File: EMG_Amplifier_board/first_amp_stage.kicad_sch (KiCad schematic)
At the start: 12 parts, among them U2 INA333xxDGK, U3 LPV821DBVR

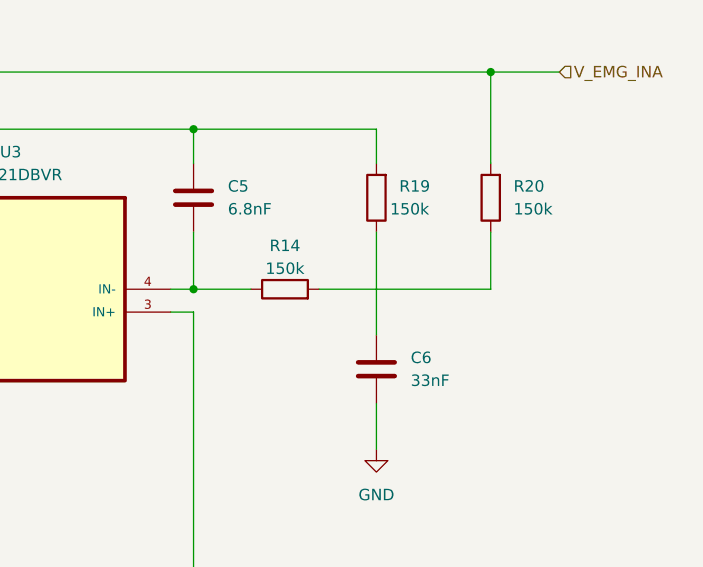
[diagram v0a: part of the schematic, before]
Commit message: correct the 400Hz LPF schematic and InAmp trace routing
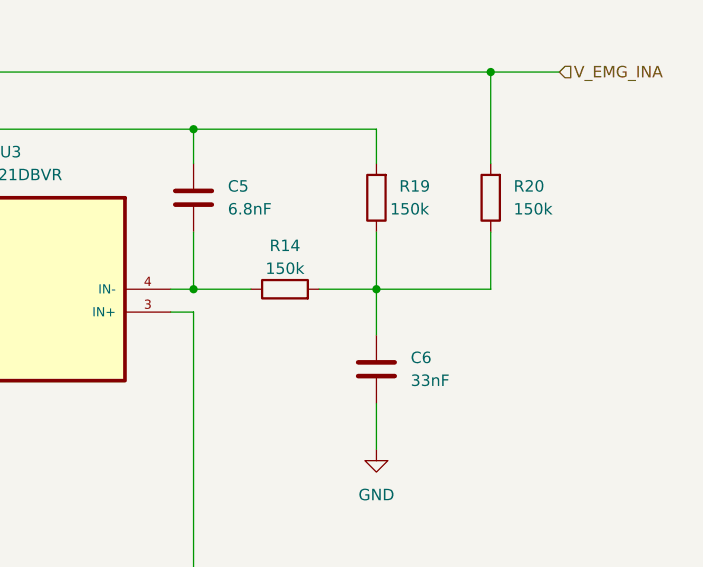
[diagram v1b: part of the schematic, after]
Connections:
- net at R14.2, R20.1: now also C6.1, R19.1
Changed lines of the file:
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@@
+	)
+	(junction
+		(at 186.69 80.01)
+		(diameter 0)
+		(color 0 0 0 0)
 	)
 	(junction
@@
 	(wire
 		(pts
+			(xy 180.34 80.01) (xy 186.69 80.01)
+		)
+		(stroke
+			(width 0)
+			(type default)
+		)
+	)
+	(wire
+		(pts
 			(xy 128.27 72.39) (xy 119.38 72.39)
 		)
@@
 	(wire
 		(pts
-			(xy 186.69 73.66) (xy 186.69 85.09)
+			(xy 186.69 73.66) (xy 186.69 80.01)
 		)
 		(stroke
@@
 	(wire
 		(pts
+			(xy 186.69 80.01) (xy 199.39 80.01)
+		)
+		(stroke
+			(width 0)
+			(type default)
+		)
+	)
+	(wire
+		(pts
 			(xy 109.22 40.64) (xy 109.22 50.8)
 		)
@@
 	(wire
 		(pts
-			(xy 180.34 80.01) (xy 199.39 80.01)
-		)
-		(stroke
-			(width 0)
-			(type default)
-		)
-	)
-	(wire
-		(pts
 			(xy 124.46 82.55) (xy 121.92 82.55)
 		)
@@
 		)
 		(stroke
+			(width 0)
+			(type default)
+		)
+	)
+	(wire
+		(pts
+			(xy 186.69 80.01) (xy 186.69 85.09)
+		)
+		(stroke

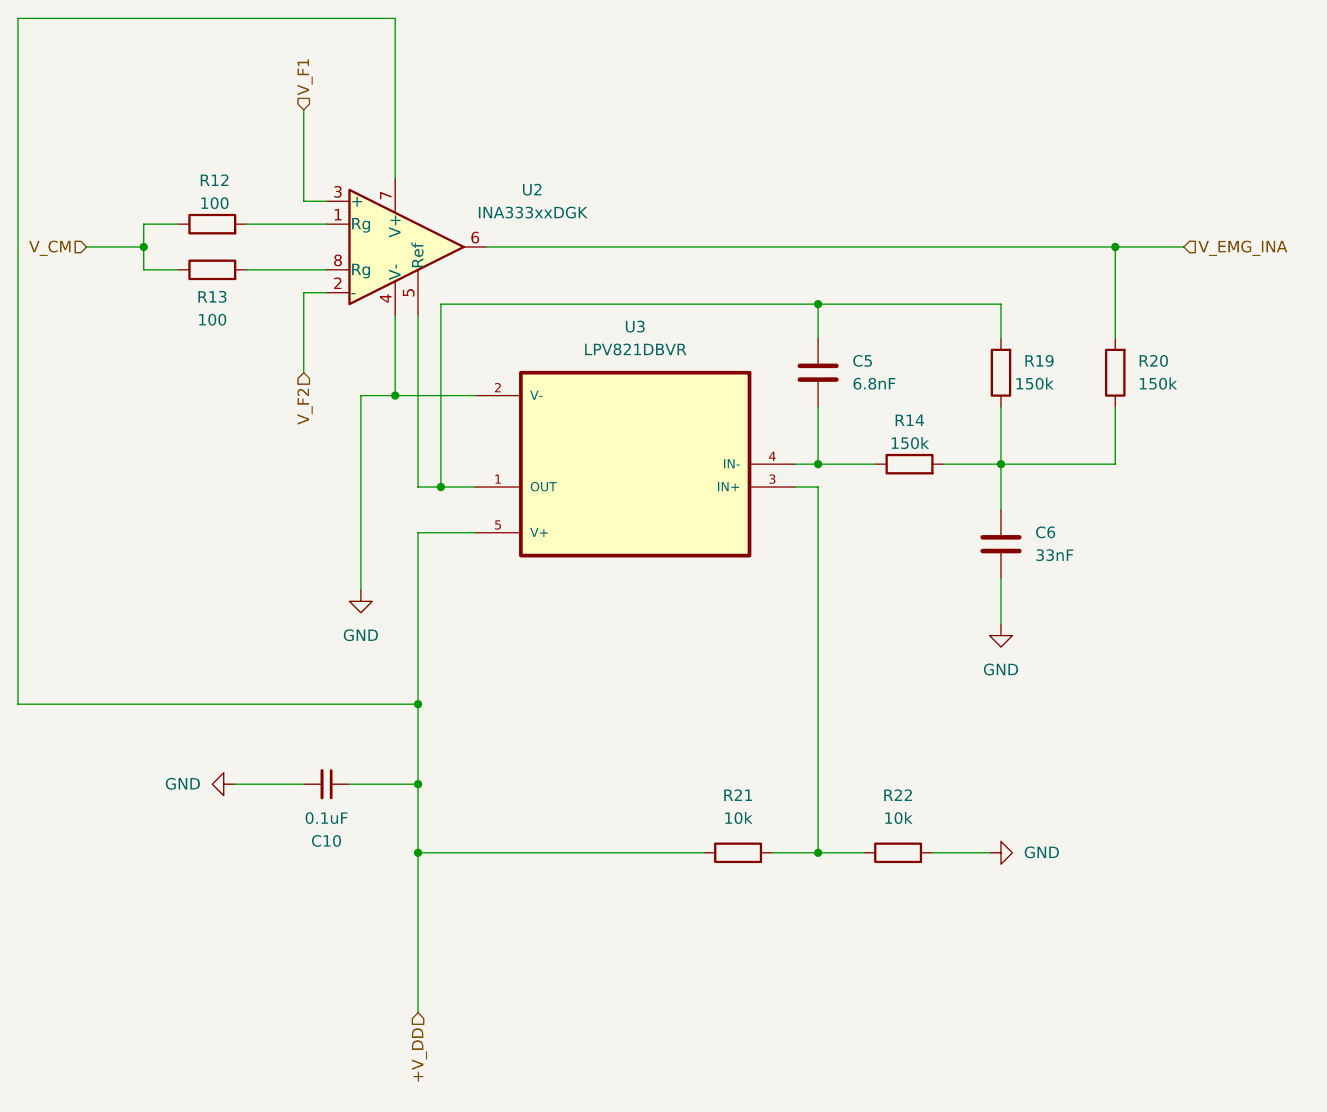
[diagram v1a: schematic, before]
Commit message: update R and C refs to correspond to paper
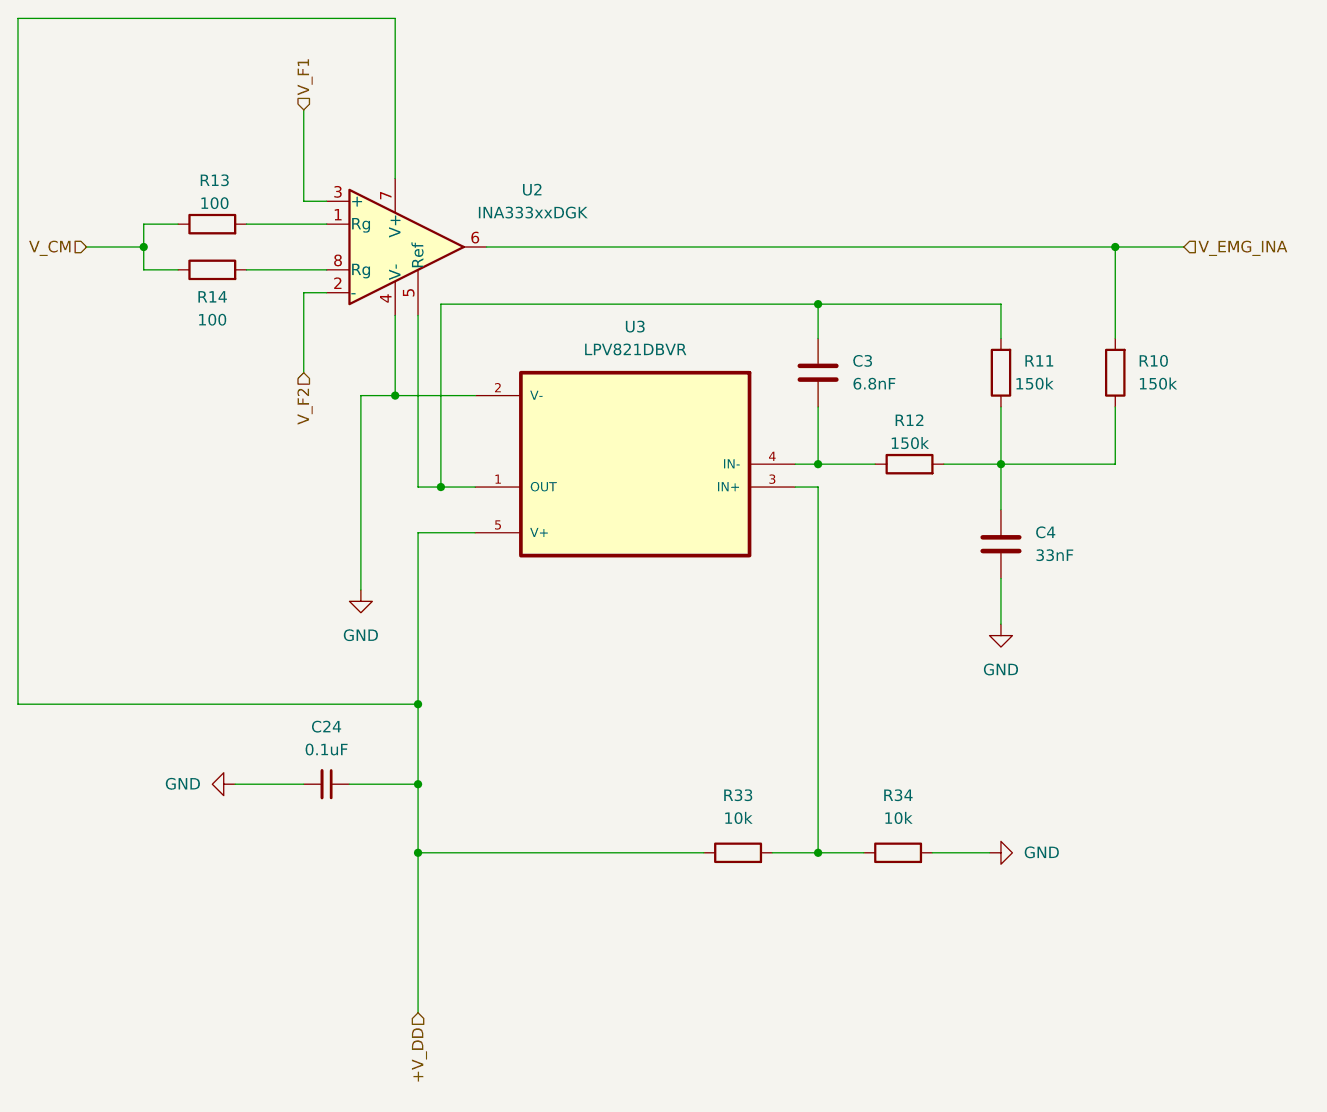
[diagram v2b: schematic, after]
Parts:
- renumbered C10 to C24, C5 to C3, C6 to C4, R20 to R10, R19 to R11, R14 to R12, R12 to R13, R13 to R14, R21 to R33, R22 to R34
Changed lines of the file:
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@@
 		(dnp no)
 		(fields_autoplaced yes)
-		(property "Reference" "R21"
+		(property "Reference" "R33"
 			(at 157.48 116.84 90)
 			(effects
@@
 			(project ""
 				(path "/26861adc-1ddf-4c37-9f8b-8db1c0839771/190e8daf-ffdb-4cbc-86a8-05377b040767/ee6da384-2a51-46fd-9ef1-0e50994f466c"
-					(reference "R21")
+					(reference "R33")
 					(unit 1)
 				)
@@
 		(on_board yes)
 		(dnp no)
-		(property "Reference" "R13"
+		(property "Reference" "R14"
 			(at 99.06 61.468 90)
 			(effects
@@
 			(project "EMG_amplifier"
 				(path "/26861adc-1ddf-4c37-9f8b-8db1c0839771/190e8daf-ffdb-4cbc-86a8-05377b040767/ee6da384-2a51-46fd-9ef1-0e50994f466c"
-					(reference "R13")
+					(reference "R14")
 					(unit 1)
 				)
@@
 		(dnp no)
 		(fields_autoplaced yes)
-		(property "Reference" "C10"
-			(at 111.7537 121.92 90)
+		(property "Reference" "C24"
+			(at 111.7536 109.22 90)
 			(effects
 				(font
@@
 		)
 		(property "Value" "0.1uF"
-			(at 111.7537 119.38 90)
+			(at 111.7536 111.76 90)
 			(effects
 				(font
@@
 			(project "EMG_amplifier"
 				(path "/26861adc-1ddf-4c37-9f8b-8db1c0839771/190e8daf-ffdb-4cbc-86a8-05377b040767/ee6da384-2a51-46fd-9ef1-0e50994f466c"
-					(reference "C10")
+					(reference "C24")
 					(unit 1)
 				)
@@
 		(dnp no)
 		(fields_autoplaced yes)
-		(property "Reference" "R22"
+		(property "Reference" "R34"
 			(at 175.26 116.84 90)
 			(effects
@@
 			(project ""
 				(path "/26861adc-1ddf-4c37-9f8b-8db1c0839771/190e8daf-ffdb-4cbc-86a8-05377b040767/ee6da384-2a51-46fd-9ef1-0e50994f466c"
-					(reference "R22")
+					(reference "R34")
 					(unit 1)
 				)
@@
 		(dnp no)
 		(fields_autoplaced yes)
-		(property "Reference" "R20"
+		(property "Reference" "R10"
 			(at 201.93 68.5799 0)
 			(effects
@@
 			(project "EMG_amplifier"
 				(path "/26861adc-1ddf-4c37-9f8b-8db1c0839771/190e8daf-ffdb-4cbc-86a8-05377b040767/ee6da384-2a51-46fd-9ef1-0e50994f466c"
-					(reference "R20")
+					(reference "R10")
 					(unit 1)
 				)
@@
 		(dnp no)
 		(fields_autoplaced yes)
-		(property "Reference" "C6"
+		(property "Reference" "C4"
 			(at 190.5 87.6299 0)
 			(effects
@@
 			(project "EMG_amplifier"
 				(path "/26861adc-1ddf-4c37-9f8b-8db1c0839771/190e8daf-ffdb-4cbc-86a8-05377b040767/ee6da384-2a51-46fd-9ef1-0e50994f466c"
-					(reference "C6")
+					(reference "C4")
 					(unit 1)
 				)
@@
 		(on_board yes)
 		(dnp no)
-		(property "Reference" "R19"
+		(property "Reference" "R11"
 			(at 189.23 68.5799 0)
 			(effects
@@
 			(project "EMG_amplifier"
 				(path "/26861adc-1ddf-4c37-9f8b-8db1c0839771/190e8daf-ffdb-4cbc-86a8-05377b040767/ee6da384-2a51-46fd-9ef1-0e50994f466c"
-					(reference "R19")
+					(reference "R11")
 					(unit 1)
 				)
@@
 		(dnp no)
 		(fields_autoplaced yes)
-		(property "Reference" "C5"
+		(property "Reference" "C3"
 			(at 170.18 68.5799 0)
 			(effects
@@
 			(project "EMG_amplifier"
 				(path "/26861adc-1ddf-4c37-9f8b-8db1c0839771/190e8daf-ffdb-4cbc-86a8-05377b040767/ee6da384-2a51-46fd-9ef1-0e50994f466c"
-					(reference "C5")
+					(reference "C3")
 					(unit 1)
 				)
@@
 		(on_board yes)
 		(dnp no)
-		(property "Reference" "R14"
+		(property "Reference" "R12"
 			(at 176.53 75.184 90)
 			(effects
@@
 			(project "EMG_amplifier"
 				(path "/26861adc-1ddf-4c37-9f8b-8db1c0839771/190e8daf-ffdb-4cbc-86a8-05377b040767/ee6da384-2a51-46fd-9ef1-0e50994f466c"
-					(reference "R14")
+					(reference "R12")
 					(unit 1)
 				)
@@
 		(on_board yes)
 		(dnp no)
-		(property "Reference" "R12"
+		(property "Reference" "R13"
 			(at 99.314 48.514 90)
 			(effects
@@
 			(project "EMG_amplifier"
 				(path "/26861adc-1ddf-4c37-9f8b-8db1c0839771/190e8daf-ffdb-4cbc-86a8-05377b040767/ee6da384-2a51-46fd-9ef1-0e50994f466c"
-					(reference "R12")
-					(unit 1)
-				)
+					(reference "R13")
+					(unit 1)
+				)

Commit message: replace 2012 capacitors with 1005
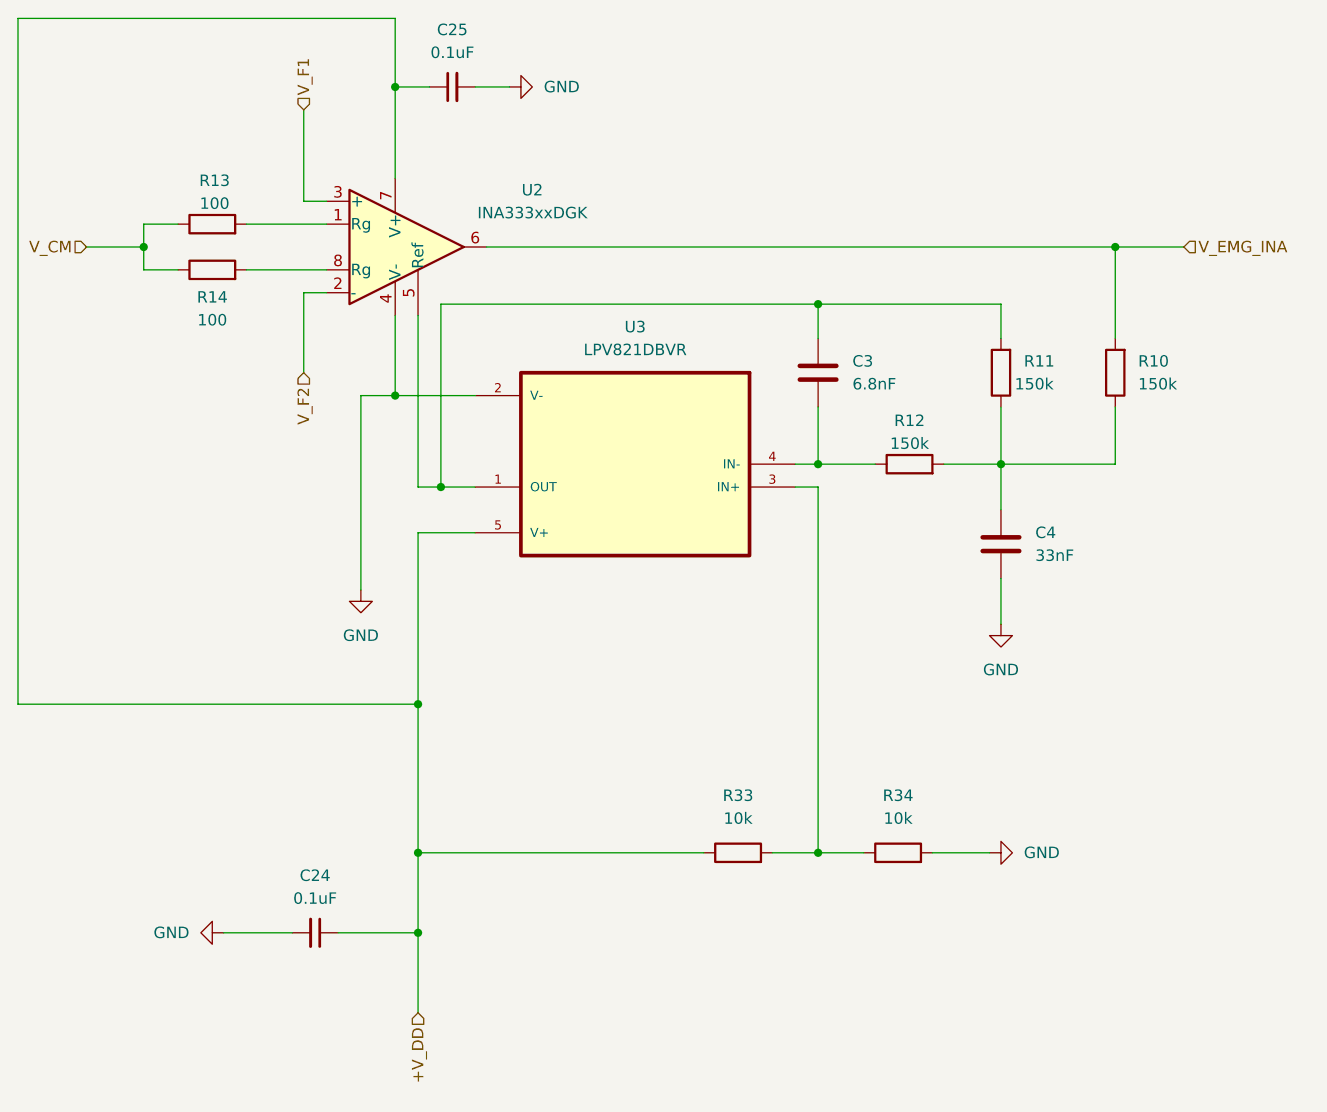
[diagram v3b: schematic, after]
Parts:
- added C25: 0.1uF, Capacitor_SMD:C_0402_1005Metric, symbol Device:C_Small
- C24: footprint Capacitor_SMD:C_0805_2012Metric -> Capacitor_SMD:C_0402_1005Metric
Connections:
- net +V_DD: now also C25.1
- net GND: now also C25.2
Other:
- moved on the sheet: C24
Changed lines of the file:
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@@
+	)
+	(junction
+		(at 121.92 132.08)
+		(diameter 0)
+		(color 0 0 0 0)
 	)
 	(junction
@@
 	)
 	(junction
-		(at 121.92 115.57)
+		(at 119.38 38.1)
 		(diameter 0)
 		(color 0 0 0 0)
@@
 	(wire
 		(pts
-			(xy 114.3 115.57) (xy 121.92 115.57)
+			(xy 119.38 38.1) (xy 119.38 48.26)
+		)
+		(stroke
+			(width 0)
+			(type default)
+		)
+	)
+	(wire
+		(pts
+			(xy 113.03 132.08) (xy 121.92 132.08)
 		)
 		(stroke
@@
 	(wire
 		(pts
-			(xy 121.92 123.19) (xy 121.92 140.97)
-		)
-		(stroke
-			(width 0)
-			(type default)
-		)
-	)
-	(wire
-		(pts
 			(xy 199.39 80.01) (xy 199.39 73.66)
 		)
@@
 	(wire
 		(pts
+			(xy 121.92 132.08) (xy 121.92 123.19)
+		)
+		(stroke
+			(width 0)
+			(type default)
+		)
+	)
+	(wire
+		(pts
 			(xy 199.39 55.88) (xy 199.39 66.04)
 		)
@@
 	(wire
 		(pts
+			(xy 121.92 132.08) (xy 121.92 140.97)
+		)
+		(stroke
+			(width 0)
+			(type default)
+		)
+	)
+	(wire
+		(pts
 			(xy 109.22 40.64) (xy 109.22 50.8)
 		)
@@
 	(wire
 		(pts
-			(xy 121.92 106.68) (xy 121.92 115.57)
-		)
-		(stroke
-			(width 0)
-			(type default)
-		)
-	)
-	(wire
-		(pts
-			(xy 119.38 30.48) (xy 119.38 48.26)
+			(xy 123.19 38.1) (xy 119.38 38.1)
+		)
+		(stroke
+			(width 0)
+			(type default)
+		)
+	)
+	(wire
+		(pts
+			(xy 119.38 30.48) (xy 119.38 38.1)
 		)
 		(stroke
@@
 	(wire
 		(pts
-			(xy 121.92 115.57) (xy 121.92 123.19)
+			(xy 121.92 106.68) (xy 121.92 123.19)
+		)
+		(stroke
+			(width 0)
+			(type default)
+		)
+	)
+	(wire
+		(pts
+			(xy 128.27 38.1) (xy 132.08 38.1)
 		)
 		(stroke
@@
 	(wire
 		(pts
-			(xy 109.22 115.57) (xy 101.6 115.57)
+			(xy 107.95 132.08) (xy 100.33 132.08)
 		)
 		(stroke
@@
 	(symbol
 		(lib_id "Device:C_Small")
-		(at 111.76 115.57 270)
+		(at 110.49 132.08 270)
 		(unit 1)
 		(exclude_from_sim no)
@@
 		(fields_autoplaced yes)
 		(property "Reference" "C24"
-			(at 111.7536 109.22 90)
+			(at 110.4836 125.73 90)
 			(effects
 				(font
@@
 		)
 		(property "Value" "0.1uF"
-			(at 111.7536 111.76 90)
-			(effects
-				(font
-					(size 1.27 1.27)
-				)
-			)
-		)
-		(property "Footprint" "Capacitor_SMD:C_0805_2012Metric"
-			(at 111.76 115.57 0)
+			(at 110.4836 128.27 90)
+			(effects
+				(font
+					(size 1.27 1.27)
+				)
+			)
+		)
+		(property "Footprint" "Capacitor_SMD:C_0402_1005Metric"
+			(at 110.49 132.08 0)
 			(effects
 				(font
@@
 		)
 		(property "Datasheet" "~"
-			(at 111.76 115.57 0)
+			(at 110.49 132.08 0)
 			(effects
 				(font
@@
 		)
 		(property "Description" "Unpolarized capacitor, small symbol"
-			(at 111.76 115.57 0)
+			(at 110.49 132.08 0)
 			(effects
 				(font
@@
 	)
 	(symbol
+		(lib_id "Device:C_Small")
+		(at 125.73 38.1 90)
+		(unit 1)
+		(exclude_from_sim no)
+		(in_bom yes)
+		(on_board yes)
+		(dnp no)
+		(fields_autoplaced yes)
+		(property "Reference" "C25"
+			(at 125.7363 31.75 90)
+			(effects
+				(font
+					(size 1.27 1.27)
+				)
+			)
+		)
+		(property "Value" "0.1uF"
+			(at 125.7363 34.29 90)
+			(effects
+				(font
+					(size 1.27 1.27)
+				)
+			)
+		)
+		(property "Footprint" "Capacitor_SMD:C_0402_1005Metric"
+			(at 125.73 38.1 0)
+			(effects
+				(font
+					(size 1.27 1.27)
+				)
+				(hide yes)
+			)
+		)
+		(property "Datasheet" "~"
+			(at 125.73 38.1 0)
+			(effects
+				(font
+					(size 1.27 1.27)
+				)
+				(hide yes)
+			)
+		)
+		(property "Description" "Unpolarized capacitor, small symbol"
+			(at 125.73 38.1 0)
+			(effects
+				(font
+					(size 1.27 1.27)
+				)
+				(hide yes)
+			)
+		)
+		(pin "1"
+		)
+		(pin "2"
+		)
+		(instances
+			(project "EMG_amplifier"
+				(path "/26861adc-1ddf-4c37-9f8b-8db1c0839771/190e8daf-ffdb-4cbc-86a8-05377b040767/ee6da384-2a51-46fd-9ef1-0e50994f466c"
+					(reference "C25")
+					(unit 1)
+				)
+			)
+		)
+	)
+	(symbol
 		(lib_id "LPV821DBVR:LPV821DBVR")
 		(at 146.05 80.01 180)
@@
 	(symbol
 		(lib_id "power:GND")
-		(at 101.6 115.57 270)
+		(at 100.33 132.08 270)
 		(unit 1)
 		(exclude_from_sim no)
@@
 		(fields_autoplaced yes)
 		(property "Reference" "#PWR010"
-			(at 95.25 115.57 0)
+			(at 93.98 132.08 0)
 			(effects
 				(font
@@
 		)
 		(property "Value" "GND"
-			(at 97.79 115.5701 90)
+			(at 96.52 132.0801 90)
 			(effects
 				(font
@@
 		)
 		(property "Footprint" ""
-			(at 101.6 115.57 0)
+			(at 100.33 132.08 0)
 			(effects
 				(font
@@
 		)
 		(property "Datasheet" ""
-			(at 101.6 115.57 0)
+			(at 100.33 132.08 0)
 			(effects
 				(font
@@
 		)
 		(property "Description" "Power symbol creates a global label with name \"GND\" , ground"
-			(at 101.6 115.57 0)
+			(at 100.33 132.08 0)
 			(effects
 				(font
@@
 					(unit 1)
 				)
+			)
+		)
+	)
+	(symbol
+		(lib_id "power:GND")
+		(at 132.08 38.1 90)
+		(unit 1)
+		(exclude_from_sim no)
+		(in_bom yes)
+		(on_board yes)
+		(dnp no)
+		(fields_autoplaced yes)
+		(property "Reference" "#PWR023"
+			(at 138.43 38.1 0)
+			(effects
+				(font
+					(size 1.27 1.27)
+				)
+				(hide yes)
+			)
+		)
+		(property "Value" "GND"
+			(at 135.89 38.0999 90)
+			(effects
+				(font
+					(size 1.27 1.27)
+				)
+				(justify right)
+			)
+		)
+		(property "Footprint" ""
+			(at 132.08 38.1 0)
+			(effects
+				(font
+					(size 1.27 1.27)
+				)
+				(hide yes)
+			)
+		)
+		(property "Datasheet" ""
+			(at 132.08 38.1 0)
+			(effects
+				(font
+					(size 1.27 1.27)
+				)
+				(hide yes)
+			)
+		)
+		(property "Description" "Power symbol creates a global label with name \"GND\" , ground"
+			(at 132.08 38.1 0)
+			(effects
+				(font
+					(size 1.27 1.27)
+				)
+				(hide yes)
+			)
+		)
+		(pin "1"
+		)
+		(instances
+			(project "EMG_amplifier"
+				(path "/26861adc-1ddf-4c37-9f8b-8db1c0839771/190e8daf-ffdb-4cbc-86a8-05377b040767/ee6da384-2a51-46fd-9ef1-0e50994f466c"
+					(reference "#PWR023")
+					(unit 1)
+				)

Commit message: minor changes
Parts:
- U3: footprint Components:SOT95P280X145-5N -> LPV821DBVR:SOT95P280X145-5N
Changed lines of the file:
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@@
 			)
 		)
-		(property "Footprint" "Components:SOT95P280X145-5N"
+		(property "Footprint" "LPV821DBVR:SOT95P280X145-5N"
 			(at 146.05 80.01 0)
 			(effects

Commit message: add buck converter 3v3 to 1v8, start new two-board sigacq project
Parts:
- U3: footprint LPV821DBVR:SOT95P280X145-5N -> Package_TO_SOT_SMD:SOT-23-5
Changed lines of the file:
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@@
 			)
 		)
-		(property "Footprint" "LPV821DBVR:SOT95P280X145-5N"
+		(property "Footprint" "Package_TO_SOT_SMD:SOT-23-5"
 			(at 146.05 80.01 0)
 			(effects
